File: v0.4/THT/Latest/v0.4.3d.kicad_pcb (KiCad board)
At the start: 2 copper layers, 100 x 100 mm, 134 parts, among them IC3 Trig Cond Socket, J1 Conn_01x05, J2 Conn_01x06, J3 Conn_01x02, J4 Conn_02x20_Counter_Clockwise, J5 Conn_01x04, J6 Conn_01x05, J8 Conn_01x03, Q1 Q_NMOS_GDS, Q2 Q_NMOS_GDS, Q3 Q_NMOS_GDS, Q4 Q_NMOS_GDS, Q5 Q_NMOS_GDSD, Q6 Q_NMOS_GDSD, U1 SP721, U2 TC4424A, U3 SP721, U4 TC4424A, U5 MPX4250, U6 ULN2003, U8 LM2940S-5.0

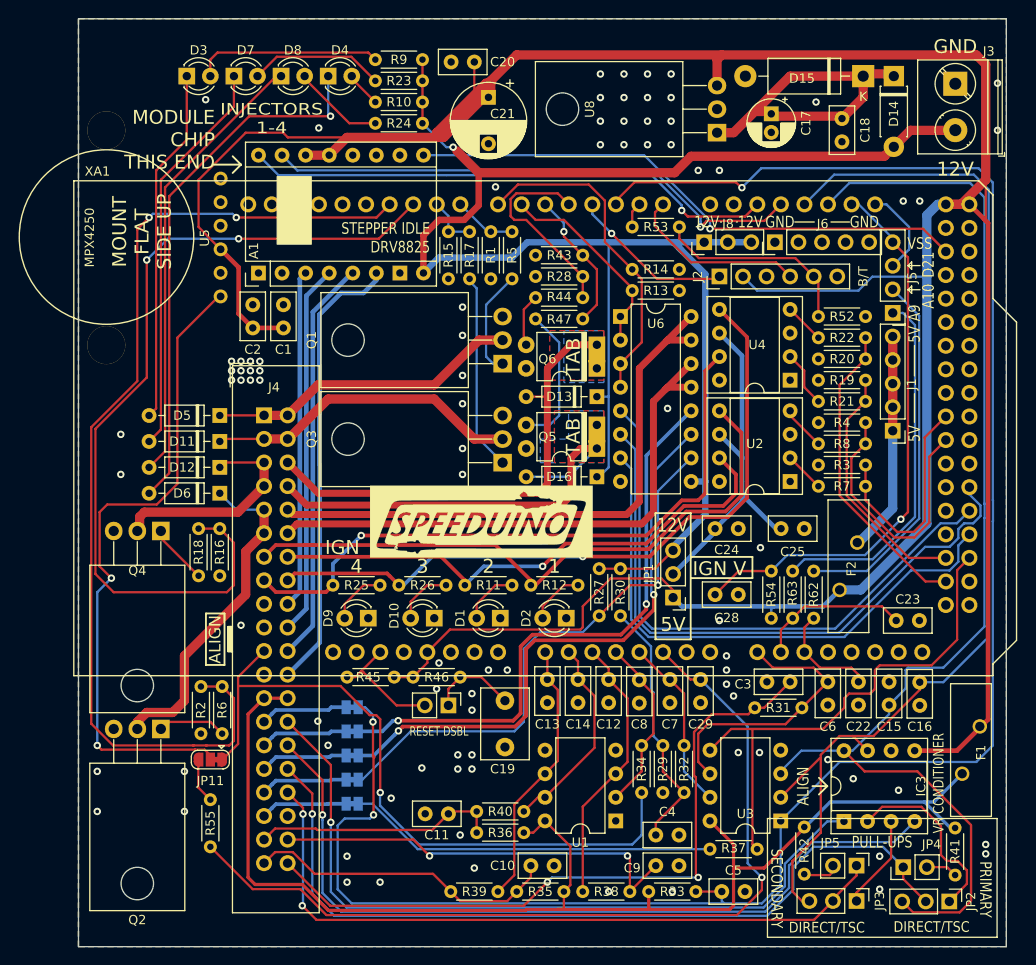
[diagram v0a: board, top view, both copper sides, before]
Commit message: add replacement MOSFETS
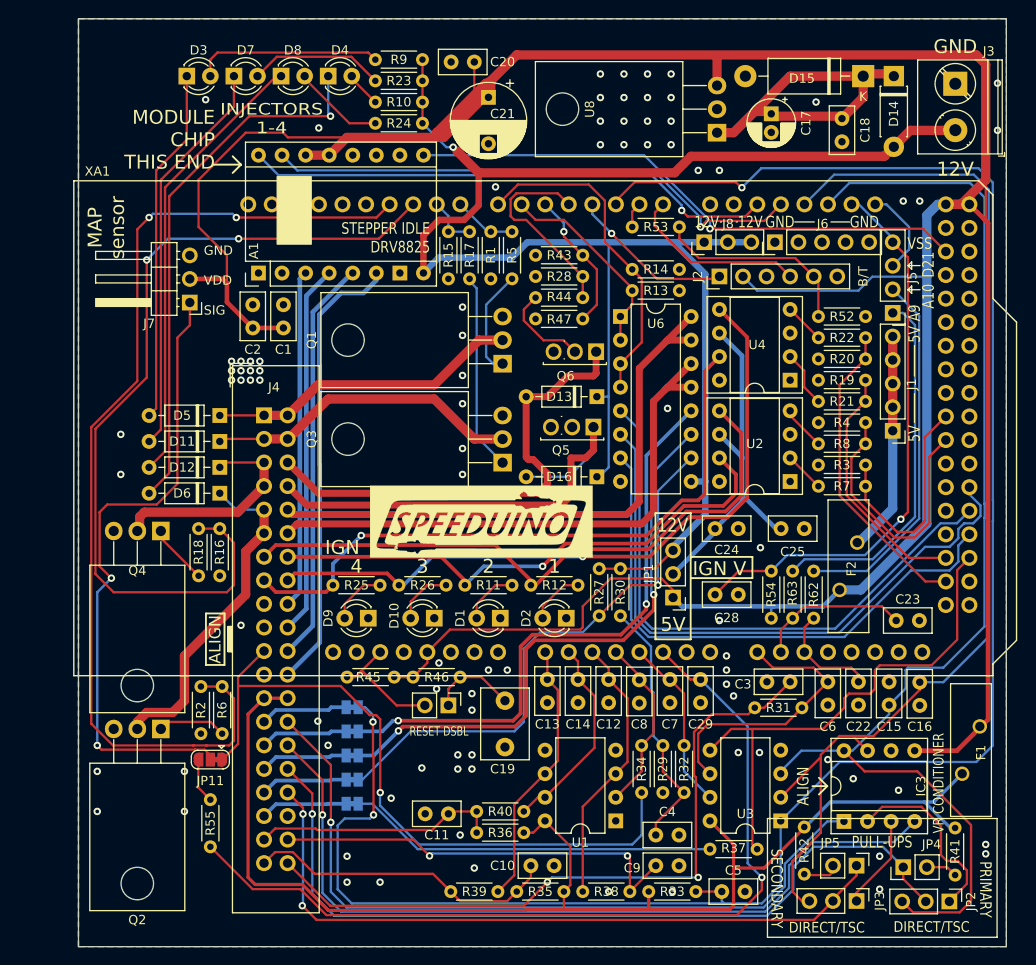
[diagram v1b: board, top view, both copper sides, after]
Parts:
- removed U5: MPX4250, Misc:MPX4250
- added J7: PinHeader_1x03_P2.54mm_Horizontal, Connector_PinHeader_2.54mm:PinHeader_1x03_P2.54mm_Horizontal, F.Cu at (122.5, 67.6)
- Q5, Q6: value Q_NMOS_GDSD -> TO-251-3_Vertical; footprint Package_DIP:Vishay_HVM-DIP-3_W7.62mm -> Package_TO_SOT_THT:TO-251-3_Vertical
- U6: value ULN2003 -> ULQ2004A
- U8: value LM2940S-5.0 -> L7805ACV
- moved Q5 2.34 mm to (166.0, 81.0)
- moved Q6 1.80 mm to (166.3, 72.9)
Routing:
- net Net-(Q5-Pad2): track 15.4 -> 0.00 mm
- net Net-(Q6-Pad2): track 5.71 -> 9.89 mm
- net VDD: track 355.9 -> 358.7 mm
- net Net-(JP11-Pad2): track 71.3 -> 69.1 mm
- net HC-2-OUT: track 53.4 -> 51.3 mm
- net IDLE-OUT: track 50.5 -> 52.2 mm
- net IGN-1-OUT: track 69.2 -> 68.2 mm
- net VDDA: track 136.4 -> 135.6 mm
- net 12V-SW: track 194.4 -> 193.8 mm
- net ADC-Clamp-11: track 30.6 -> 30.1 mm
- removed copper zone on B.Cu, net HC-2-OUT
- removed copper zone on F.Cu, net HC-2-OUT
- removed copper zone on B.Cu, net IDLE-OUT
- removed copper zone on F.Cu, net IDLE-OUT
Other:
- net class Default removed
- board text added: "Diarmuid Kelly 2025"
- board text added: "GND VDD SIG"
- board text added: "MAP sensor"
- board text added: "Speeduino v0.4.3d(v2)"
- board text removed: "MOUNT FLAT SIDE UP"
- board text removed: "Speeduino v0.4.3d"
- board text removed: "TAB"
